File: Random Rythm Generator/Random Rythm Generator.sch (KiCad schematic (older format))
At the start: 23 parts, among them SW1 SW_Push, U1 LM78L05_TO92, U2 40106, U3 4040, U4 74LS165

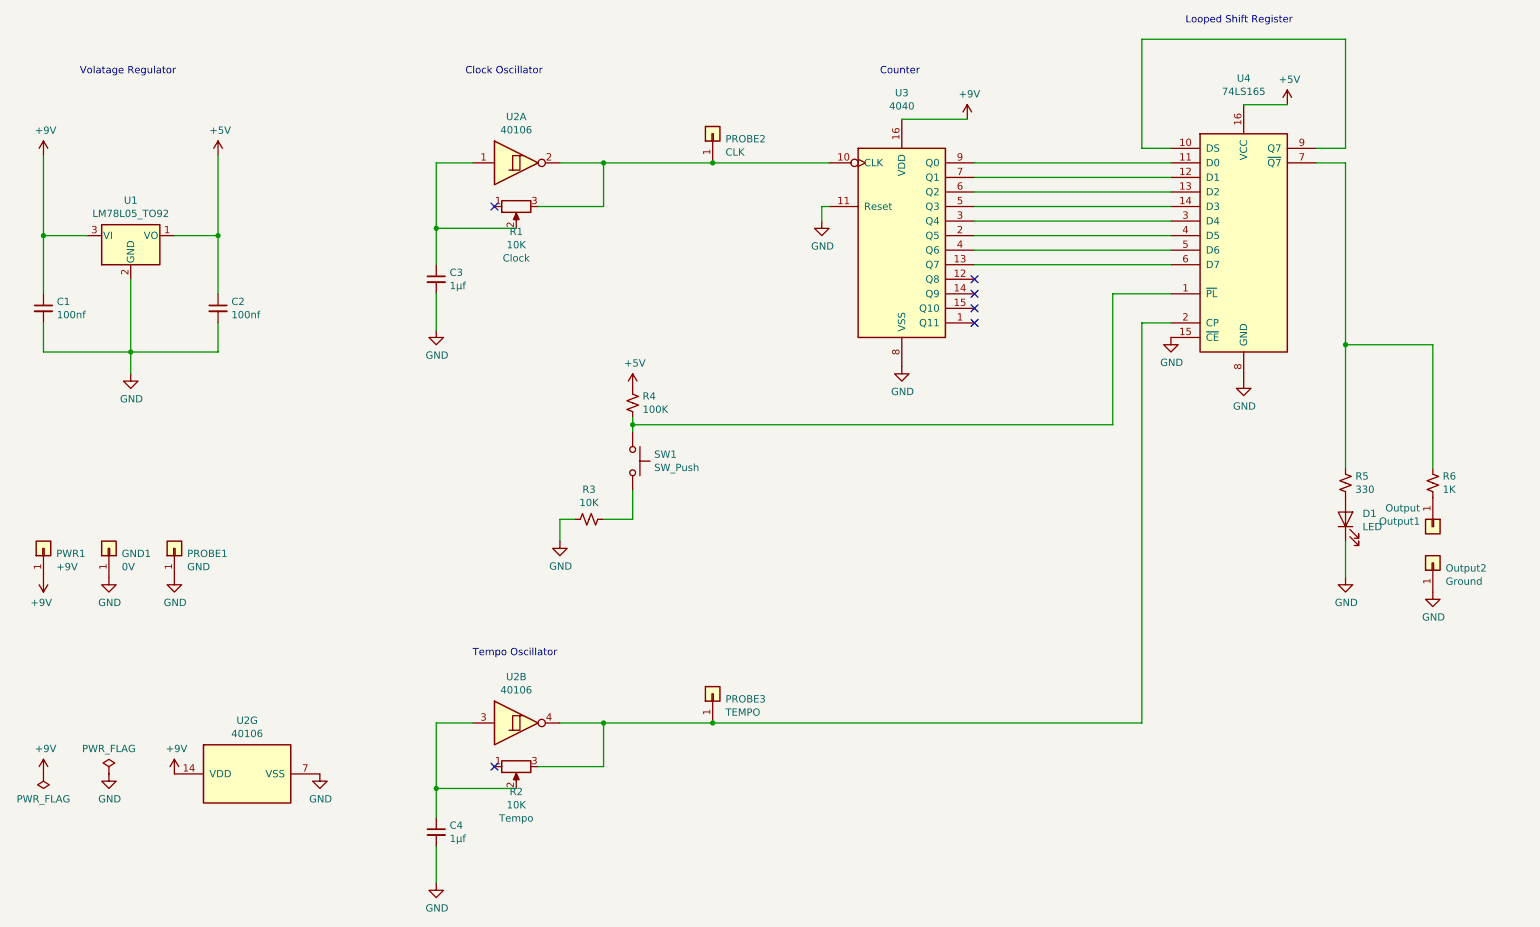
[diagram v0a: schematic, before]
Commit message: add smoothing capacitor to power supply
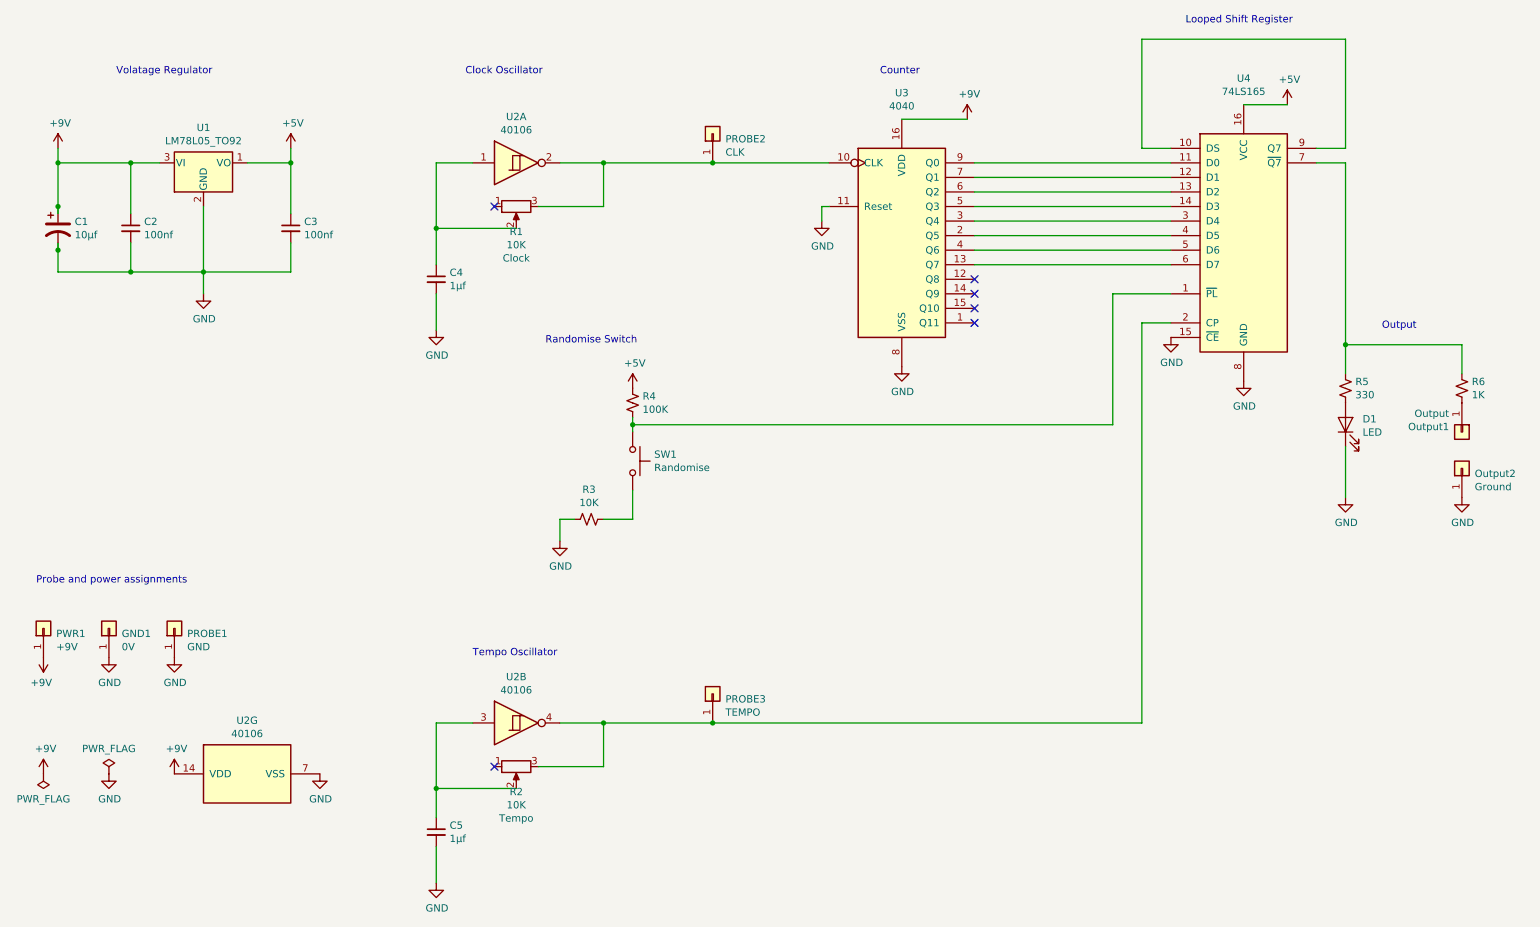
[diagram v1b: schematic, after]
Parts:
- removed C1: 100nf, Capacitor_THT:C_Disc_D5.0mm_W2.5mm_P5.00mm, symbol Device:C_Small
- added C1: 10µf, Capacitor_THT:C_Radial_D8.0mm_H7.0mm_P3.50mm, symbol Device:CP1
- added C2: 100nf, Capacitor_THT:C_Disc_D5.0mm_W2.5mm_P5.00mm, symbol Device:C_Small
- PROBE1: footprint TestPoint:TestPoint_THTPad_2.5x2.5mm_Drill1.2mm -> TestPoint:TestPoint_Pad_2.5x2.5mm
- SW1: value SW_Push -> Randomise
- renumbered C2 to C3, C3 to C4, C4 to C5
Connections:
- wire segments 66 -> 72
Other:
- note added: "Output"
- note added: "Probe and power assignments"
- note added: "Randomise Switch"
- moved on the sheet: C3, D1, GND1, Output1, Output2, PROBE1, PWR1, R5, R6, U1

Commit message: neaten schematic and pcb layout slightly
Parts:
- R1, R2: symbol Device:R_POT -> Device:R_POT_US
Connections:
- wire segments 72 -> 70
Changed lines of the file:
@@
 Wire Wire Line
 	1950 2850 1950 2700
-Wire Wire Line
-	6200 2350 6200 2250
-Wire Wire Line
-	6200 2250 6250 2250
 $Comp
 L Connector_Generic:Conn_01x01 PWR1
@@
 L power:GND #PWR015
 U 1 1 5D2F13E6
-P 6200 2350
-F 0 "#PWR015" H 6200 2100 50  0001 C CNN
-F 1 "GND" H 6205 2177 50  0000 C CNN
-F 2 "" H 6200 2350 50  0001 C CNN
-F 3 "" H 6200 2350 50  0001 C CNN
-	1    6200 2350
+P 6250 2250
+F 0 "#PWR015" H 6250 2000 50  0001 C CNN
+F 1 "GND" H 6255 2077 50  0000 C CNN
+F 2 "" H 6250 2250 50  0001 C CNN
+F 3 "" H 6250 2250 50  0001 C CNN
+	1    6250 2250
 	1    0    0    -1
 $EndComp
@@
 Wire Wire Line
 	3550 3100 3550 2850
-Wire Wire Line
-	7200 1650 6750 1650
 $Comp
 L power:+9V #PWR03
@@
 L power:+9V #PWR017
 U 1 1 5D328148
-P 7200 1650
-F 0 "#PWR017" H 7200 1500 50  0001 C CNN
-F 1 "+9V" H 7215 1823 50  0000 C CNN
-F 2 "" H 7200 1650 50  0001 C CNN
-F 3 "" H 7200 1650 50  0001 C CNN
-	1    7200 1650
+P 7050 1650
+F 0 "#PWR017" H 7050 1500 50  0001 C CNN
+F 1 "+9V" H 7065 1823 50  0000 C CNN
+F 2 "" H 7050 1650 50  0001 C CNN
+F 3 "" H 7050 1650 50  0001 C CNN
+	1    7050 1650
 	1    0    0    -1
 $EndComp
@@
 Looped Shift Register
 $Comp
-L Device:R_POT R1
+L Device:R_POT_US R1
 U 1 1 5D2030A8
 P 4100 2250
@@
 	4250 6100 4700 6100
 $Comp
-L Device:R_POT R2
+L Device:R_POT_US R2
 U 1 1 5D211D4D
 P 4100 6100
@@
 	0    1    1    0
 $EndComp
+Wire Wire Line
+	6750 1650 7050 1650
 $EndSCHEMATC

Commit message: minor PCB and schematic tweaks
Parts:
- C2: value 100nf -> 330nf
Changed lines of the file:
@@
 P 1450 2400
 F 0 "C2" H 1542 2446 50  0000 L CNN
-F 1 "100nf" H 1542 2355 50  0000 L CNN
+F 1 "330nf" H 1542 2355 50  0000 L CNN
 F 2 "Capacitor_THT:C_Disc_D5.0mm_W2.5mm_P5.00mm" H 1450 2400 50  0001 C CNN
 F 3 "~" H 1450 2400 50  0001 C CNN
